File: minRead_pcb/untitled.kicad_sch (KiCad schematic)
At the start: 8 parts, among them J7 Micro_SD_Card

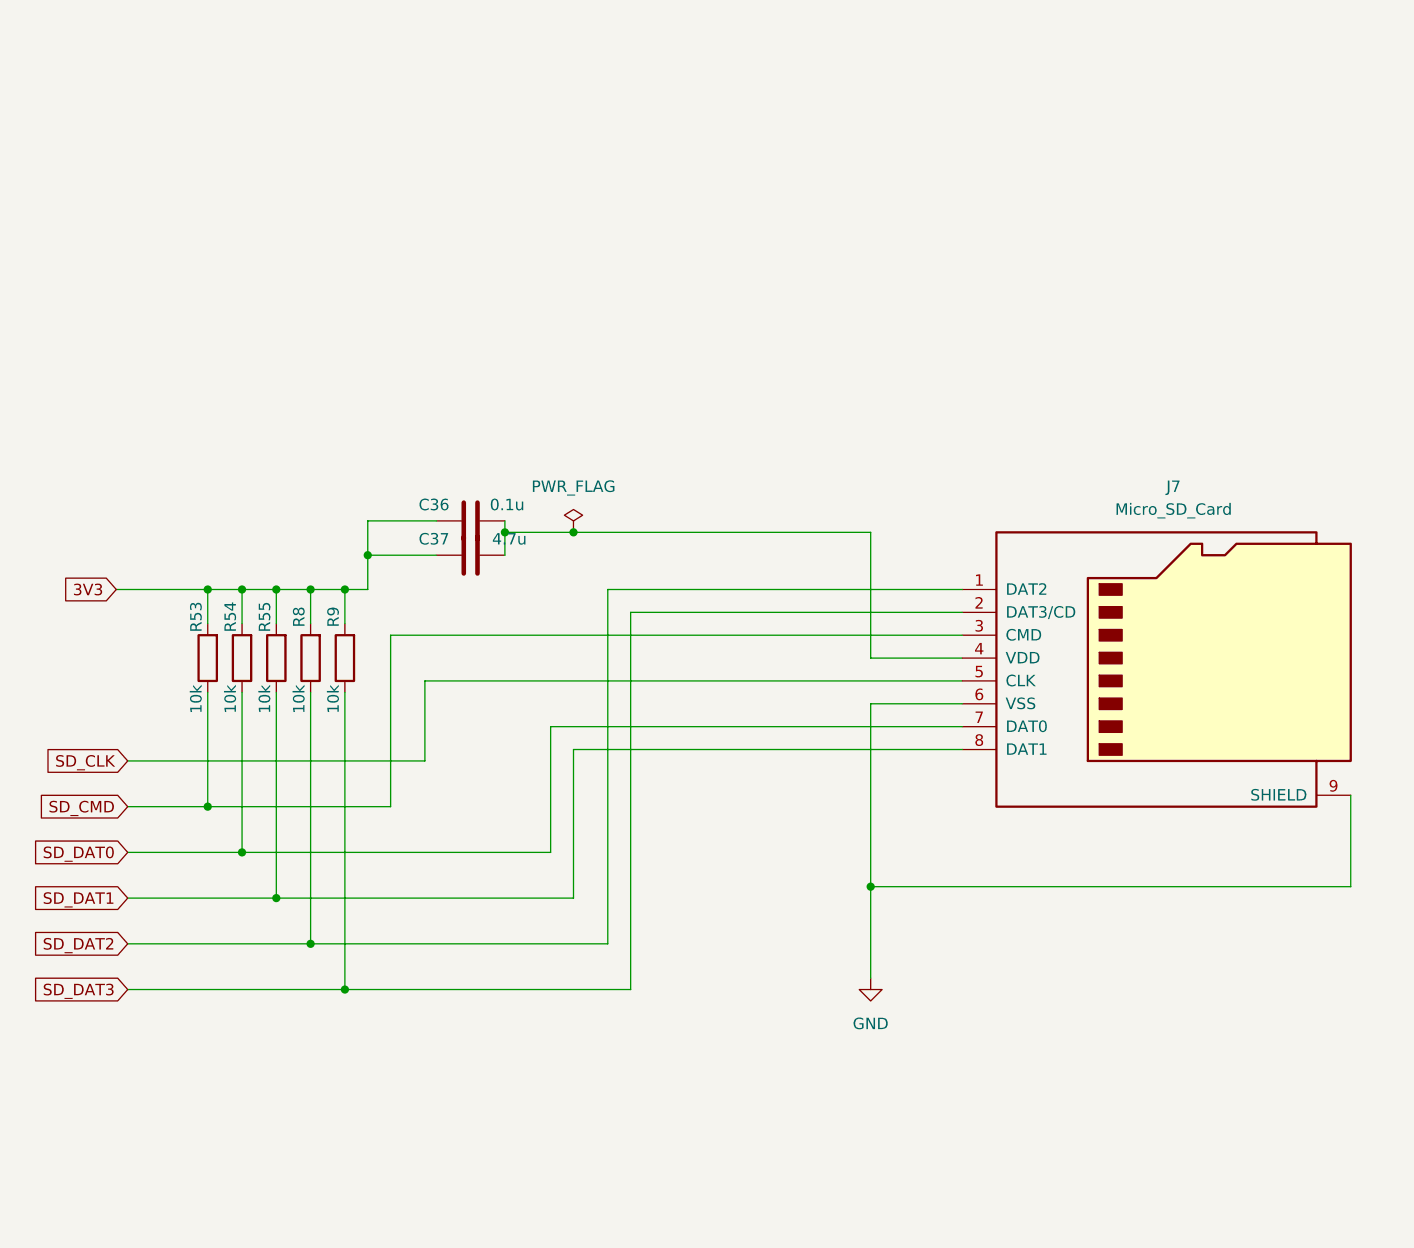
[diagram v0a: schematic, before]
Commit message: - schematic updates: - usb500 mode enabled on bq - charge limit set to 100mA 8.9kohm (safe for small batteries) - series resistors on sd card and epd lines - esd arrays for usb-c and sd-card - increased output cap for ldo from 4.7u to 22u - added pgood to gpio - confirmed reverse polarity stuff - cap to ground instead of series for sd card vdd - fixed cap values on epd
new layout:
- adjusted board size
- very compact
- need to fill ground planes and check drc errors (a lot because of solder mask)
- need to adjust jst footprint in case there's a better choice
- review review review
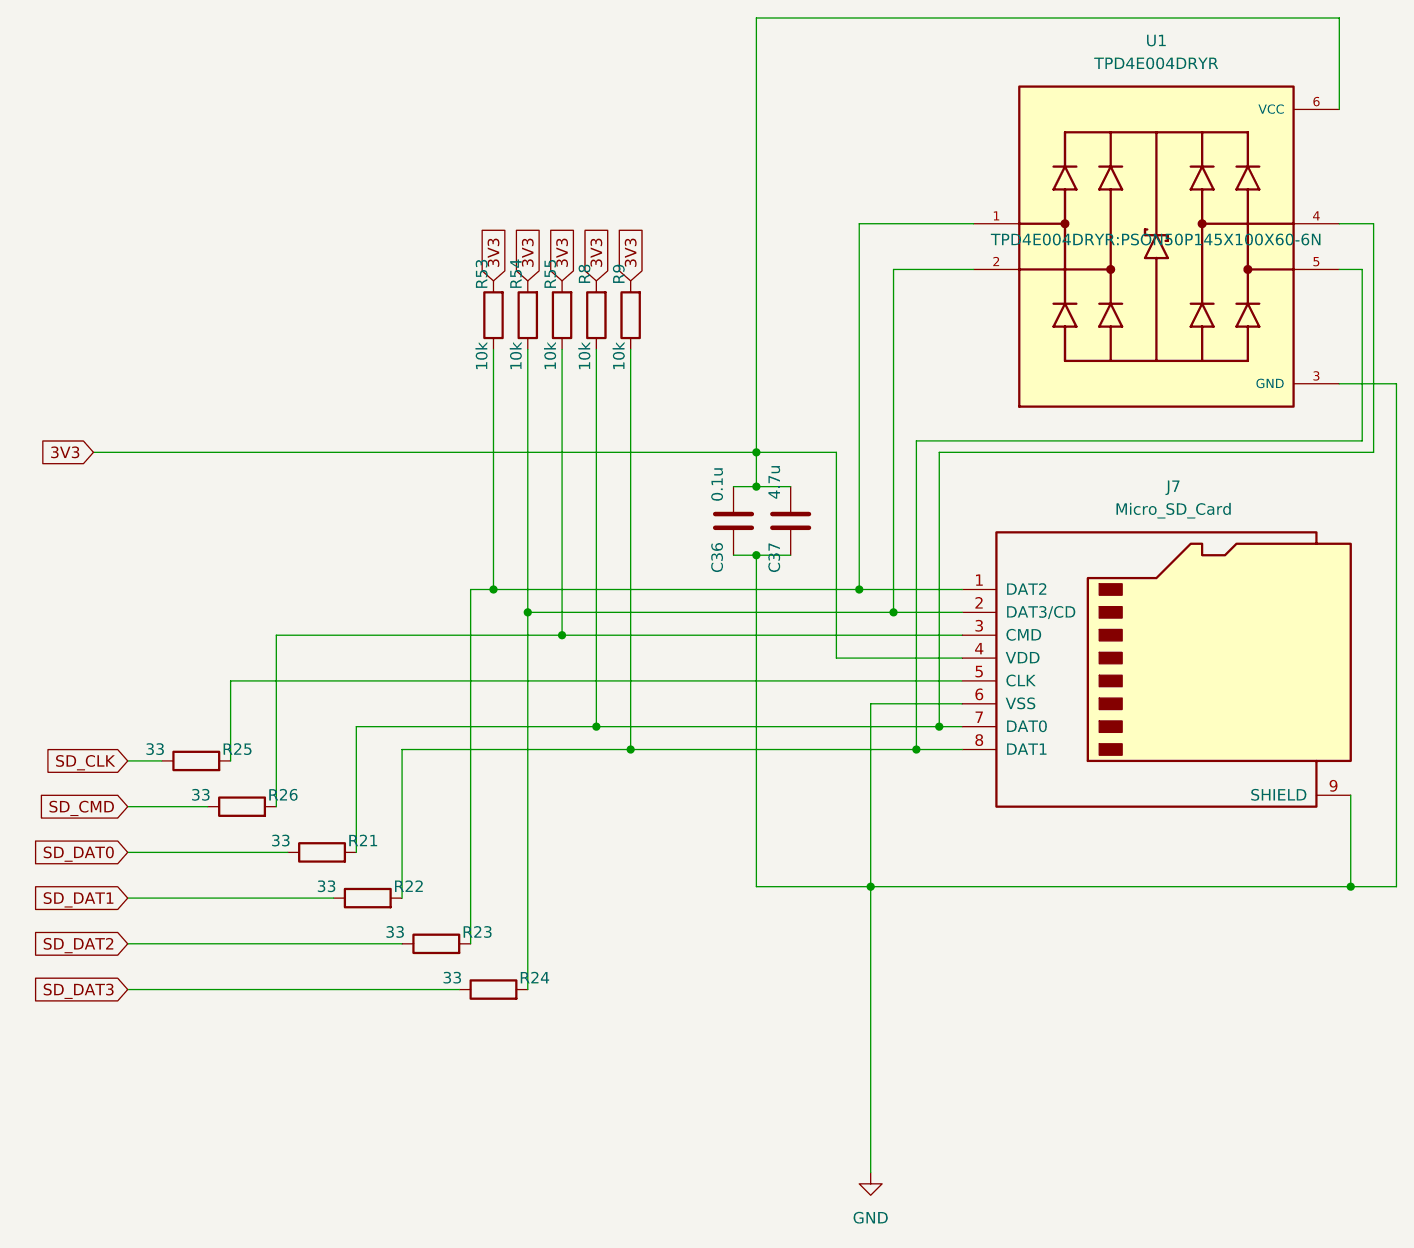
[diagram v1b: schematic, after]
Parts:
- added R21, R22, R23, R24, R25, R26: 33, Resistor_SMD:R_0805_2012Metric_Pad1.20x1.40mm_HandSolder, symbol Device:R
- added U1: TPD4E004DRYR, TPD4E004DRYR:PSON50P145X100X60-6N, symbol TPD4E004DRYR:TPD4E004DRYR
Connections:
- net 3V3: now also C36.2, C37.2, J7.4 (VDD), U1.6 (VCC); no longer C36.1, C37.1
- net GND: now also C36.1, C37.1, U1.3 (GND)
- net SD_CLK: now also R25.1; no longer J7.5 (CLK)
- net SD_CMD: now also R26.1; no longer J7.3 (CMD), R53.1
- net SD_DAT0: now also R21.1; no longer J7.7 (DAT0), R54.1
- net SD_DAT1: now also R22.1; no longer J7.8 (DAT1), R55.1
- net SD_DAT2: now also R23.1; no longer J7.1 (DAT2), R8.1
- net SD_DAT3: now also R24.1; no longer J7.2 (DAT3/CD), R9.1
- new net: J7.1 (DAT2), R23.2, R53.1, U1.1
- new net: J7.7 (DAT0), R21.2, R8.1, U1.4
- new net: J7.2 (DAT3/CD), R24.2, R54.1, U1.2
- new net: J7.8 (DAT1), R22.2, R9.1, U1.5
- new net: J7.3 (CMD), R26.2, R55.1
- new net: J7.5 (CLK), R25.2
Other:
- moved on the sheet: C36, C37, R53, R54, R55, R8, R9

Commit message: gigantic commit, my bad revised schematic to sanity check turns out my fpc was flipped, now fixed added following schematics: - battery protection circuit - series LED driver - external peripheral connector for unused GPIO revised following schematics: - power path, replaced with mcp charger and FET rather than bq - buttons, opted for resistor ladder circuit, added two more for xte compatibility - eink driver, opted to change to updated components from waveshare 2.3 - updated esd components for usb-c and sdmmc - updated usb-c receptacle, now through-hole
New layout:
- mostly same as last time, but work done to ensure good grounding for LED/eink circuits
- eink gpio has minimal crossing/coupling just in case
- esp32 and 24 pin headers have longer pads hopefully for easier soldering
- external header in corner back of device
- prettier passive component layout
- fat 3v3 traces and small zone fill

- todo:
- DRC errors, mostly clearance and silkscreen overlap
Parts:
- removed C36: 0.1u, Capacitor_SMD:C_0805_2012Metric_Pad1.18x1.45mm_HandSolder, symbol Device:C
- removed C37: 4.7u, Capacitor_SMD:C_0805_2012Metric_Pad1.18x1.45mm_HandSolder, symbol Device:C
- removed J7: Micro_SD_Card, Connector_Card:microSD_HC_Hirose_DM3AT-SF-PEJM5, symbol Connector:Micro_SD_Card
- removed R21, R22, R23, R24, R25, R26: 33, Resistor_SMD:R_0805_2012Metric_Pad1.20x1.40mm_HandSolder, symbol Device:R
- removed R53, R54, R55, R8, R9: 10k, Resistor_SMD:R_0805_2012Metric_Pad1.20x1.40mm_HandSolder, symbol Device:R
- removed U1: TPD4E004DRYR, TPD4E004DRYR:PSON50P145X100X60-6N, symbol TPD4E004DRYR:TPD4E004DRYR
